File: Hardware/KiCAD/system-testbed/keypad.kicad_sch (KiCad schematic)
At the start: 43 parts, among them J5 HW-834 Module, SW23 1, SW24 4, SW25 7, SW26 *, SW27 2, SW28 5, SW29 8, SW30 0, SW31 3, SW32 6, SW33 9, SW34 #, SW35 UP, SW36 DOWN, SW37 LEFT, SW38 RIGHT, SW39 PTT, SW40 MENU, SW41 EXIT, SW42 SK0

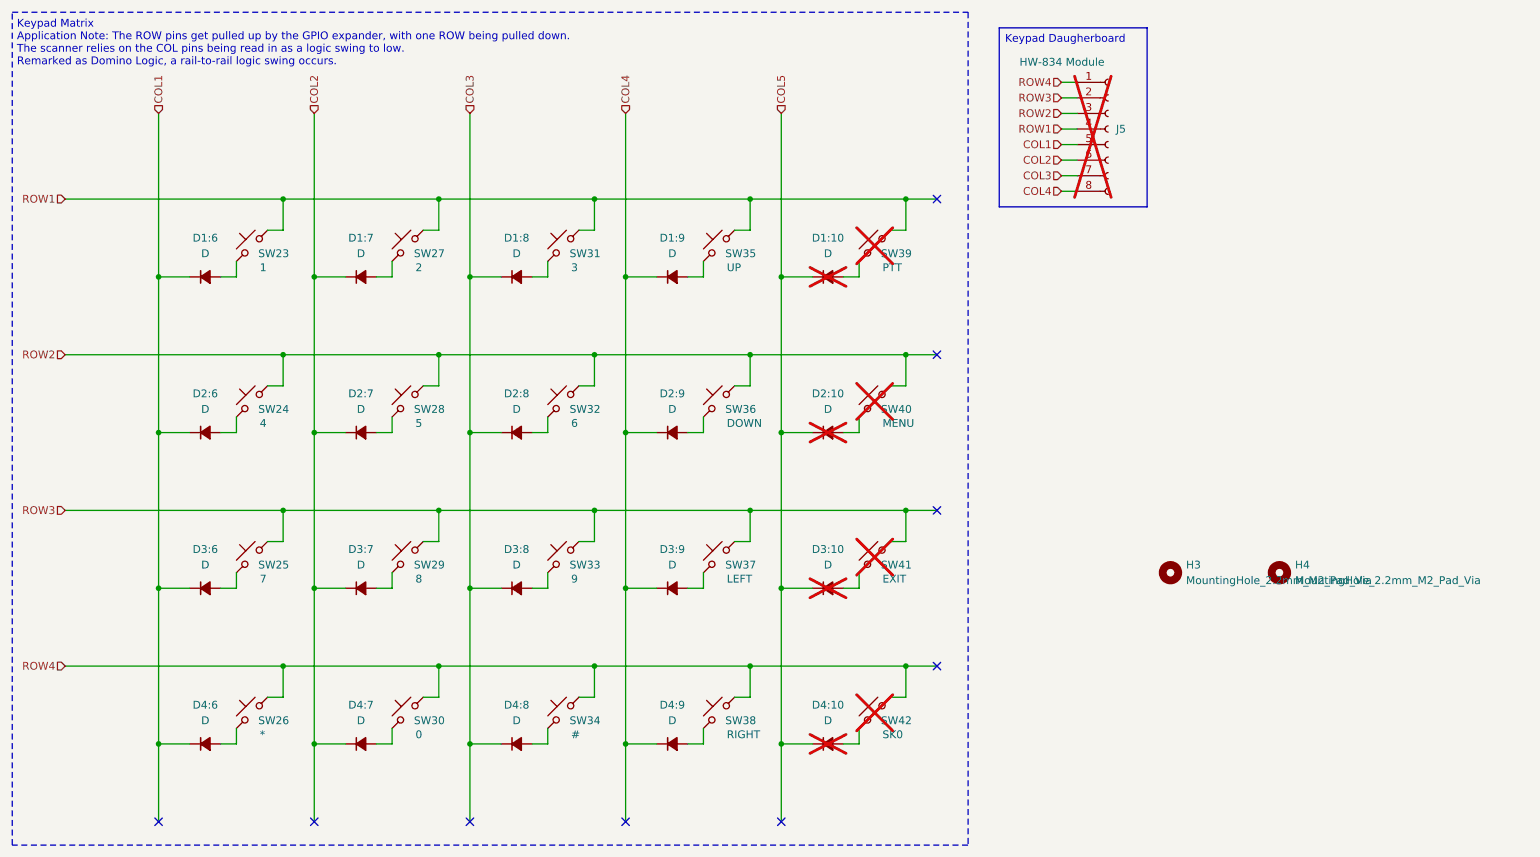
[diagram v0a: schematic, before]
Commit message: fix: reannotate schematics for pcb editor use #55
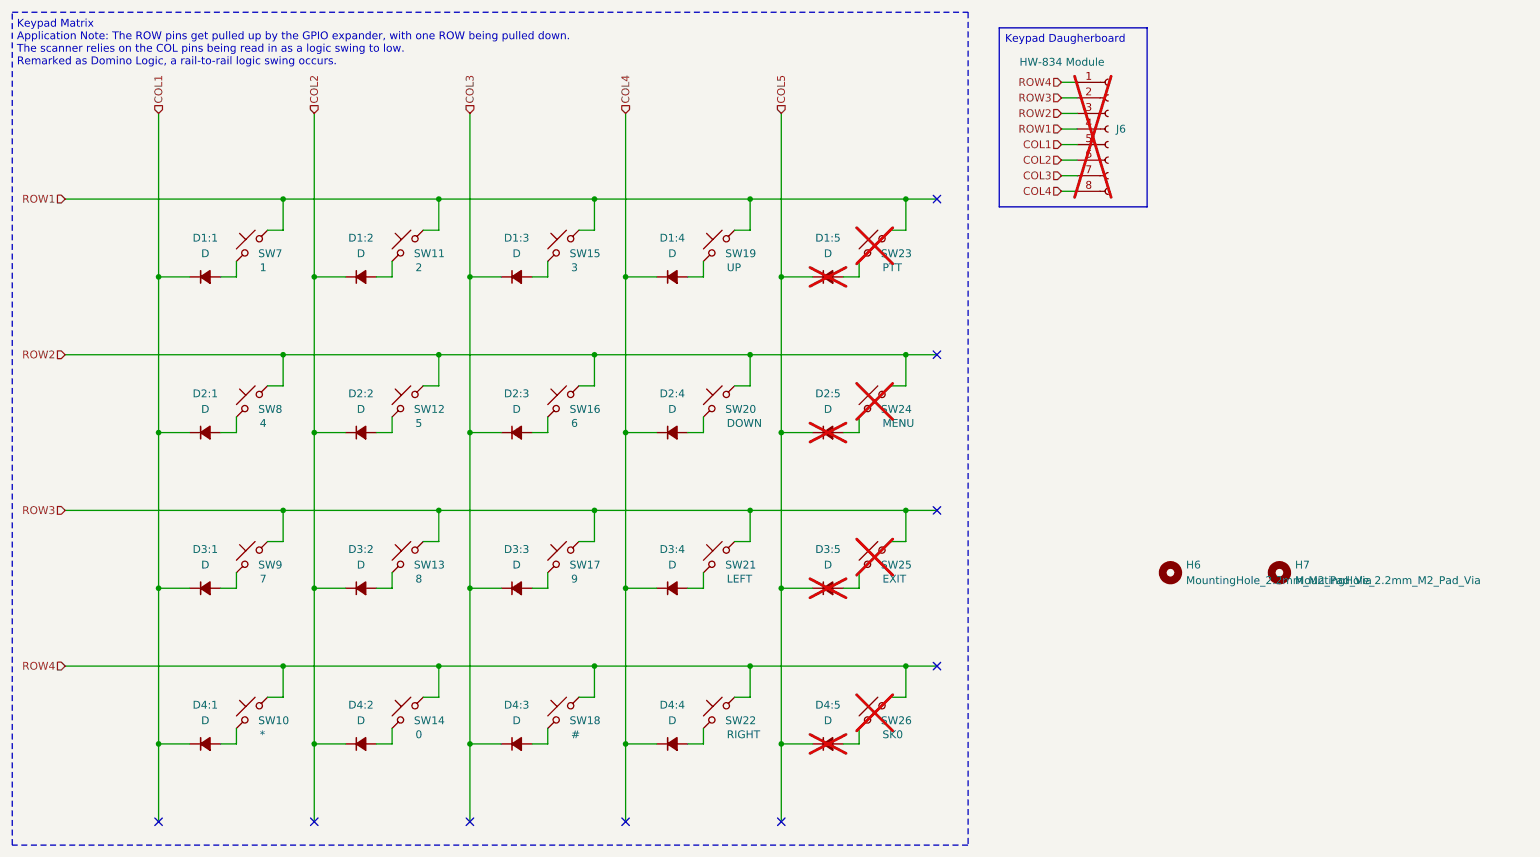
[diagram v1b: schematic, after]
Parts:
- renumbered D1:6 to D1:1, D1:7 to D1:2, D1:8 to D1:3, D1:9 to D1:4, D1:10 to D1:5, D2:6 to D2:1, D2:7 to D2:2, D2:8 to D2:3, D2:9 to D2:4, D2:10 to D2:5, D3:6 to D3:1, D3:7 to D3:2, D3:8 to D3:3, D3:9 to D3:4, D3:10 to D3:5, D4:6 to D4:1, D4:7 to D4:2, D4:8 to D4:3, D4:9 to D4:4, D4:10 to D4:5, H3 to H6, H4 to H7, J5 to J6, SW26 to SW10, SW27 to SW11, SW28 to SW12, SW29 to SW13, SW30 to SW14, SW31 to SW15, SW32 to SW16, SW33 to SW17, SW34 to SW18, SW35 to SW19, SW36 to SW20, SW37 to SW21, SW38 to SW22, SW39 to SW23, SW40 to SW24, SW41 to SW25, SW42 to SW26, SW23 to SW7, SW24 to SW8, SW25 to SW9
